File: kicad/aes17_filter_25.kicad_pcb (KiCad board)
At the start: 2 copper layers, 193 x 92.6 mm, 38 parts, among them J1 NC3FAAH, J2 NC3MAAH, J3 Conn_01x01_Pin, J4 Conn_01x01_Pin, SW1 SW_DPST, SW2 SW_DPDT_x2

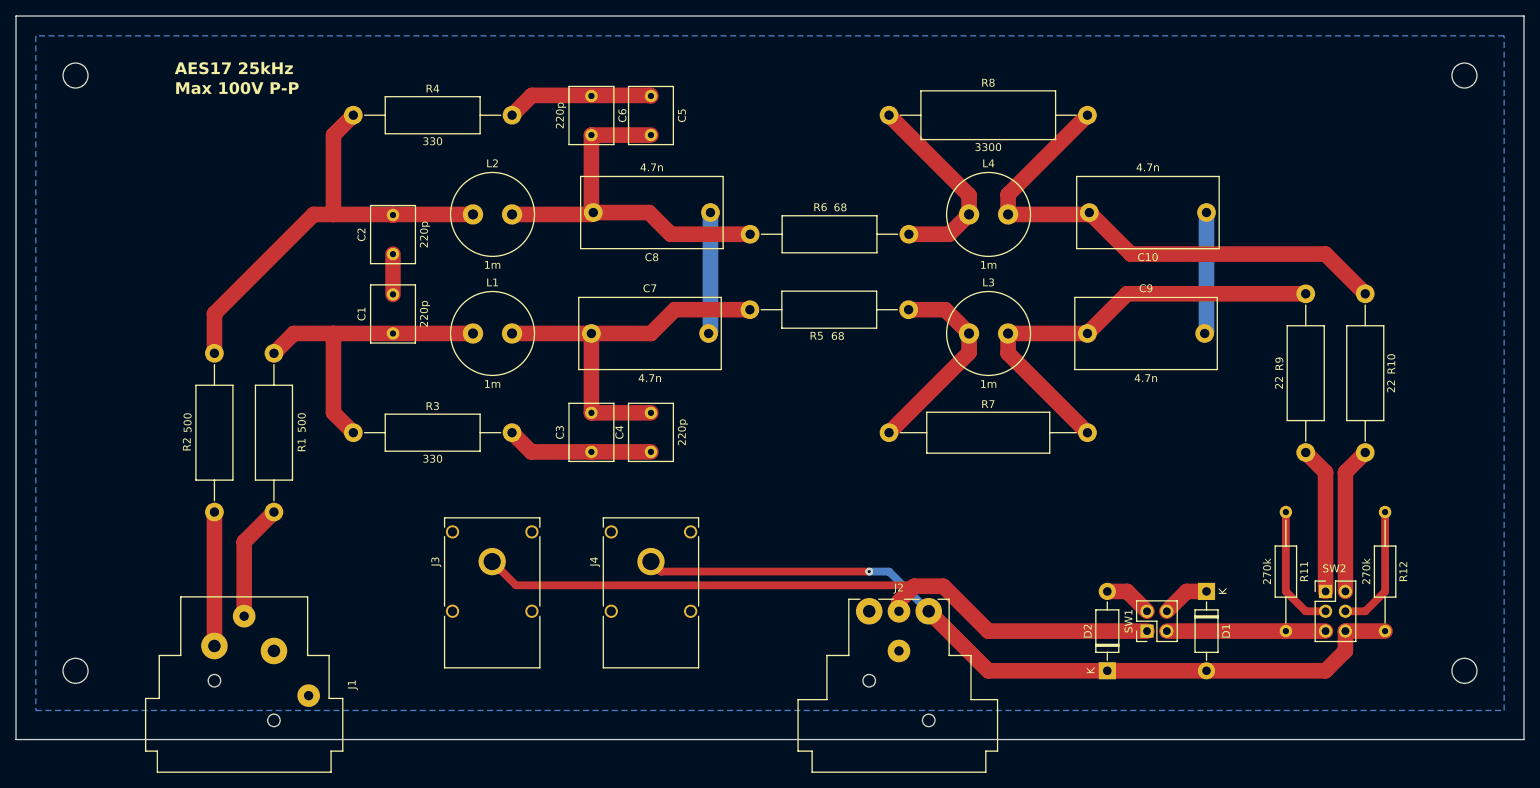
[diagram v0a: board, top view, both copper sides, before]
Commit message: Added GND connections to capacitor mid-points
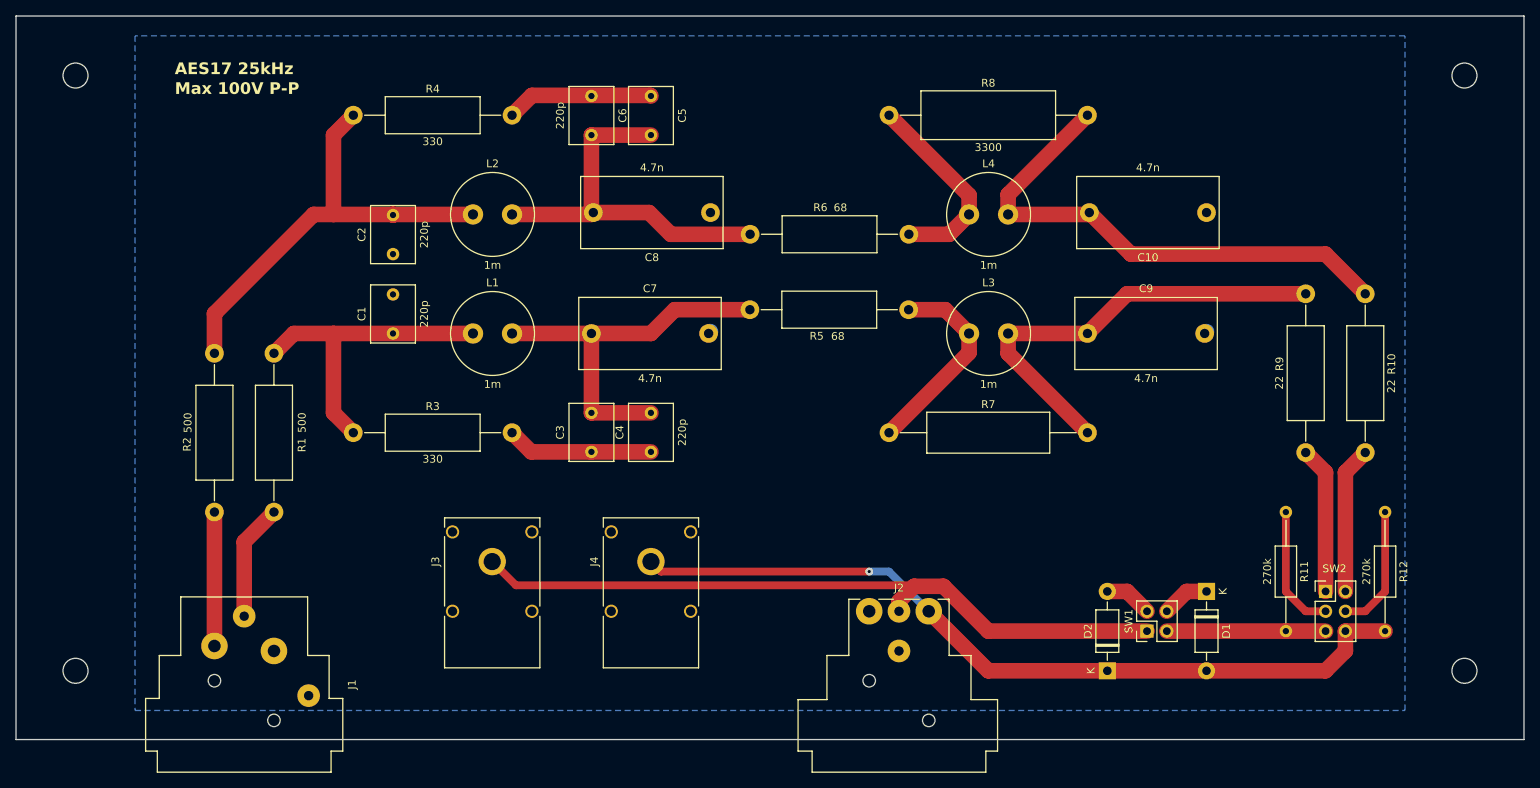
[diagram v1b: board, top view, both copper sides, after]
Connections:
- C1 pad 2: Net-(C1-Pad2) -> GND
- C10 pad 1: Net-(C10-Pad1) -> GND
- C2 pad 1: Net-(C1-Pad2) -> GND
- C7 pad 2: Net-(C7-Pad2) -> GND
- C8 pad 1: Net-(C7-Pad2) -> GND
- C9 pad 2: Net-(C10-Pad1) -> GND
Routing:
- net Net-(C7-Pad2): track 15.6 -> 0.00 mm
- net Net-(C10-Pad1): track 15.6 -> 0.00 mm
- net Net-(C1-Pad2): track 5.16 -> 0.00 mm
- net GND: track 0.00 -> 0.68 mm

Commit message: Readme updated
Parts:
- J1: value NC3FAAH -> NC3FAAH2
- R7: footprint Resistor_THT:R_Axial_DIN0516_L15.5mm_D5.0mm_P25.40mm_Horizontal -> Resistor_THT:R_Axial_DIN0414_L11.9mm_D4.5mm_P20.32mm_Horizontal
- R8: footprint Resistor_THT:R_Axial_DIN0617_L17.0mm_D6.0mm_P25.40mm_Horizontal -> Resistor_THT:R_Axial_DIN0414_L11.9mm_D4.5mm_P20.32mm_Horizontal
- moved H1 3.59 mm to (58.4, 55.9)
- moved H2 2.54 mm to (233.7, 55.9)
- moved H3 2.54 mm to (58.4, 129.5)
- moved R7 2.54 mm to (162.6, 99.1)
- moved R8 2.54 mm to (162.6, 58.4)
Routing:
- net Net-(SW2B-B): track 18.8 -> 22.9 mm
- net Net-(SW2A-B): track 18.8 -> 22.9 mm
- net Net-(SW2B-C): track 16.3 -> 12.3 mm
- net Net-(SW2A-C): track 16.3 -> 12.3 mm
- net Net-(C10-Pad2): track 67.0 -> 69.0 mm
- net Net-(L3-Pad1): track 25.9 -> 27.9 mm
- net Net-(L4-Pad1): track 25.7 -> 27.6 mm
- net Net-(C9-Pad1): track 57.1 -> 59.0 mm
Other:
- board size 193 x 92.6 mm -> 190 x 90 mm
- board text added: "AES17 25KHz 0.1dB variation 20Hz-40KHz -55dB at 250KHz Max 100V P-P into any load Max 200V P-P into R500+ (c) Matt Clark 2023 CERN-OHL-W PCB 190x90mm"
- board text removed: "AES17 25kHz"
- board text removed: "Max 100V P-P"

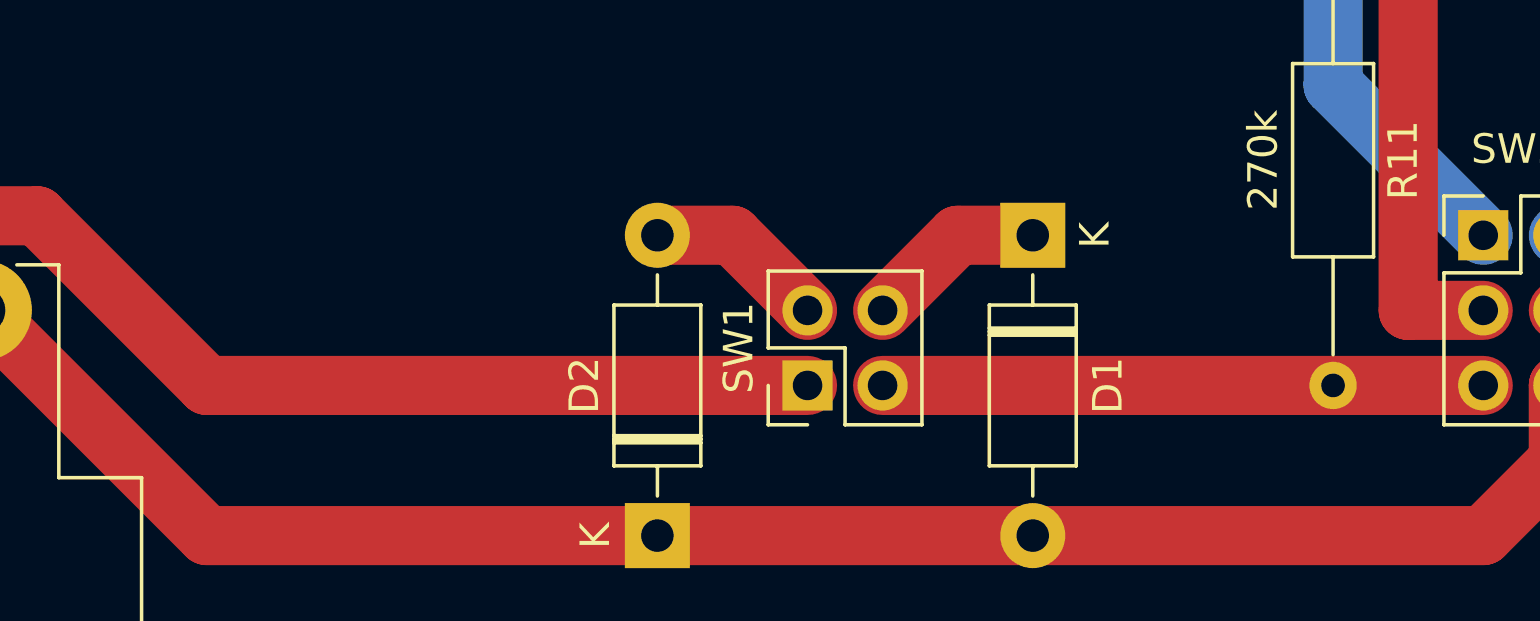
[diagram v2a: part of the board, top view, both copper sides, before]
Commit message: simplified diode switch to 1pst, fixed R7 and R8 footprints
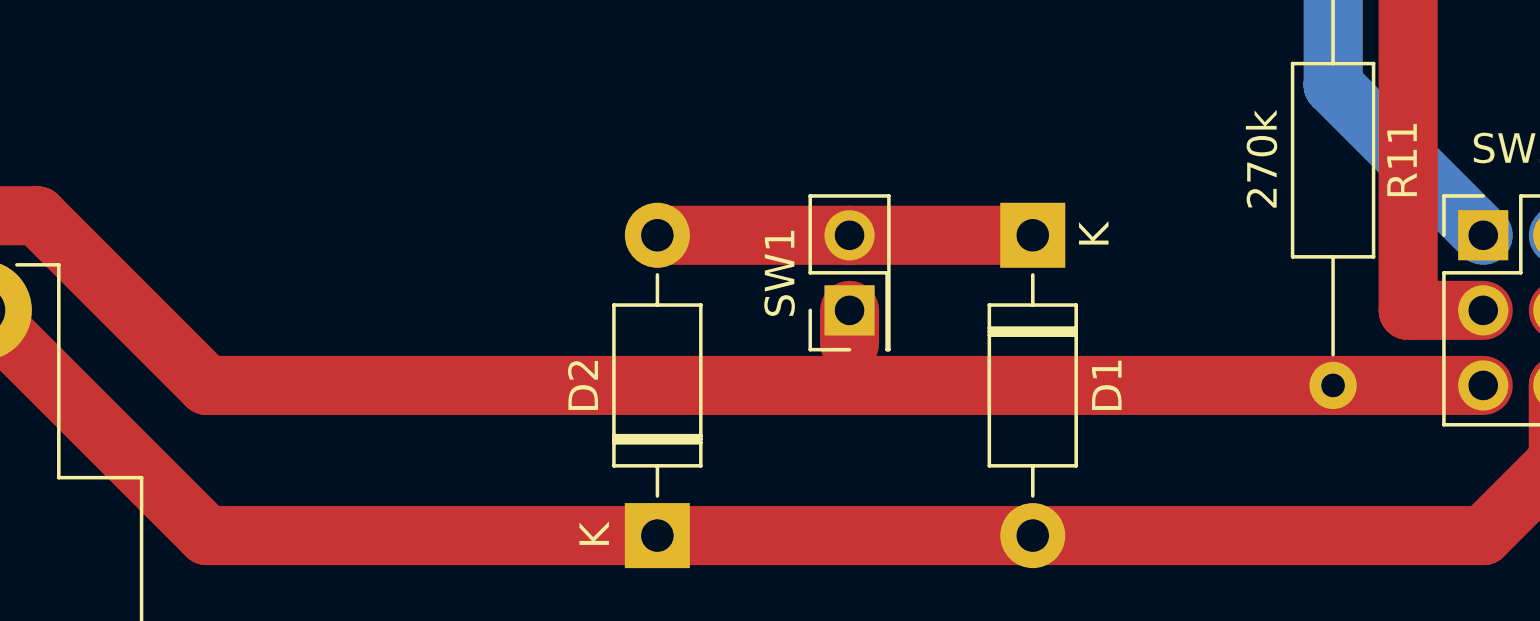
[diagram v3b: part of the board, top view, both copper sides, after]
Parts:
- J1: value NC3FAAH2 -> NC3FAAH
- SW1: value SW_DPST -> SW_SPST; footprint Connector_PinHeader_2.54mm:PinHeader_2x02_P2.54mm_Vertical -> Connector_PinHeader_2.54mm:PinHeader_2x01_P2.54mm_Vertical
- moved SW1 2.91 mm to (194.5, 121.9)
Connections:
- D2 pad 2: Net-(D2-A) -> Net-(D1-K)
- J1 pad G: unconnected-(J1-PadG) -> GND
- J2 pad G: unconnected-(J2-PadG) -> GND
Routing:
- net Net-(D1-K): track 6.13 -> 12.7 mm
- net Net-(D2-A): track 6.13 -> 0.00 mm
- net Net-(J3-Pin_1): track 112.9 -> 116.6 mm

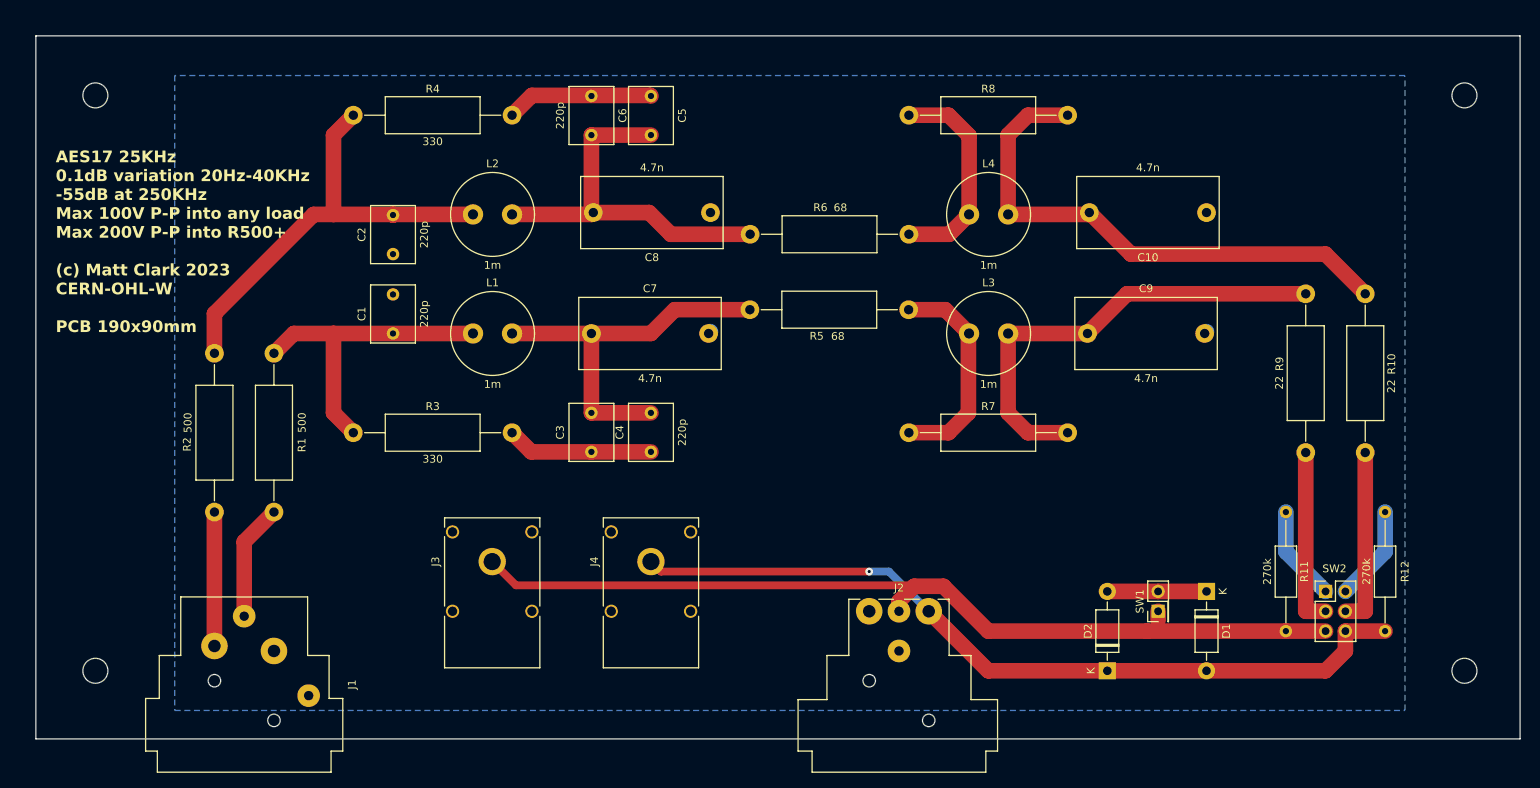
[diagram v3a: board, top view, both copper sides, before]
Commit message: Removed protection diodes, updated readme
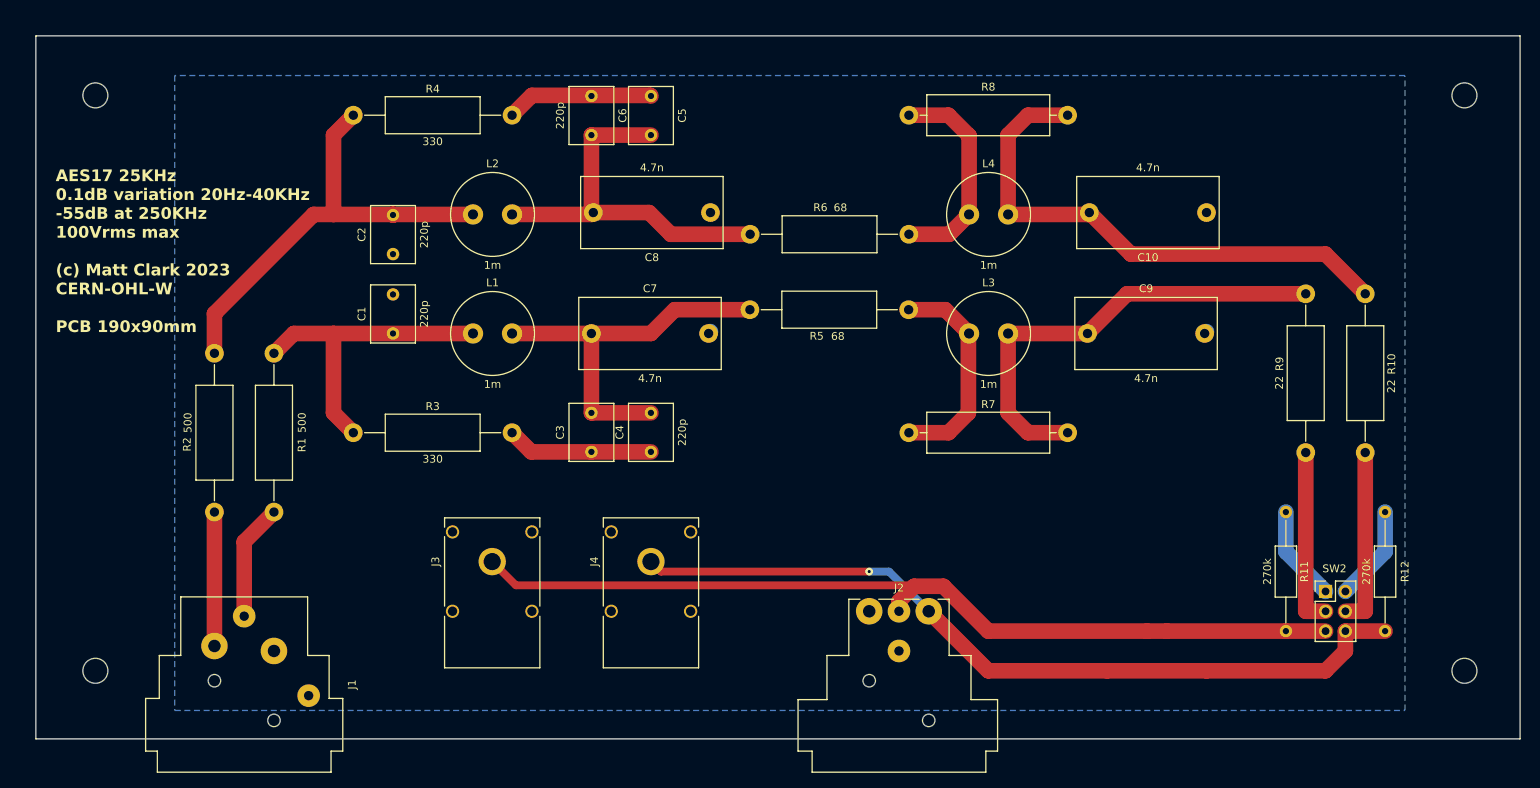
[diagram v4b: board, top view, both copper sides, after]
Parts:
- removed D1, D2: D_Zener, Diode_THT:D_DO-41_SOD81_P10.16mm_Horizontal
- removed SW1: SW_SPST, Connector_PinHeader_2.54mm:PinHeader_2x01_P2.54mm_Vertical
- R7, R8: footprint Resistor_THT:R_Axial_DIN0414_L11.9mm_D4.5mm_P20.32mm_Horizontal -> Resistor_THT:R_Axial_DIN0516_L15.5mm_D5.0mm_P20.32mm_Horizontal
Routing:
- net Net-(D1-K): track 12.7 -> 0.00 mm
- net Net-(J3-Pin_1): track 116.6 -> 115.4 mm
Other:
- board text added: "AES17 25KHz 0.1dB variation 20Hz-40KHz -55dB at 250KHz 100Vrms max (c) Matt Clark 2023 CERN-OHL-W PCB 190x90mm"
- board text removed: "AES17 25KHz 0.1dB variation 20Hz-40KHz -55dB at 250KHz Max 100V P-P into any load Max 200V P-P into R500+ (c) Matt Clark 2023 CERN-OHL-W PCB 190x90mm"

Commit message: Shrank board width, added images, updated readme
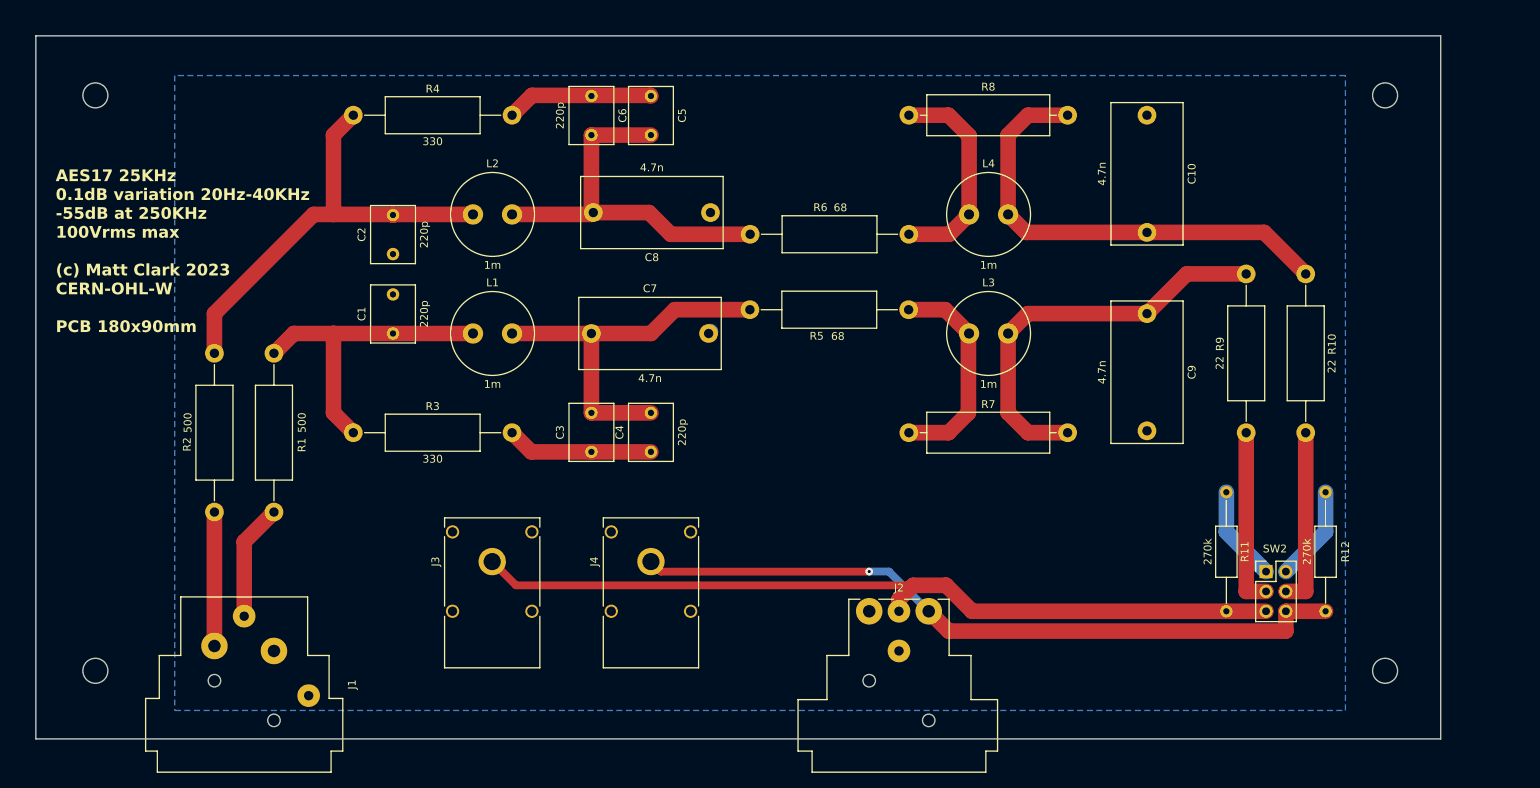
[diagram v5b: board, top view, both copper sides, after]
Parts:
- moved C10 14.6 mm to (193.0, 58.4), turned to -90 degrees
- moved H2 10.2 mm to (223.5, 55.9)
- moved H4 10.2 mm to (223.5, 129.5)
- moved C9 8.03 mm to (193.0, 83.8), turned to -90 degrees
- moved R9 8.03 mm to (205.7, 78.7)
- moved R11 8.03 mm to (203.2, 106.7)
- moved R12 8.03 mm to (215.9, 106.7)
- moved SW2 8.03 mm to (208.3, 116.8)
- moved R10 8.03 mm to (213.4, 78.7)
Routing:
- net Net-(J4-Pin_1): track 103.4 -> 92.6 mm
- net Net-(J3-Pin_1): track 115.4 -> 105.8 mm
- net Net-(C10-Pad2): track 69.0 -> 60.1 mm
- net Net-(C9-Pad1): track 59.0 -> 52.5 mm
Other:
- board size 190 x 90 mm -> 179.8 x 90 mm
- board text added: "AES17 25KHz 0.1dB variation 20Hz-40KHz -55dB at 250KHz 100Vrms max (c) Matt Clark 2023 CERN-OHL-W PCB 180x90mm"
- board text removed: "AES17 25KHz 0.1dB variation 20Hz-40KHz -55dB at 250KHz 100Vrms max (c) Matt Clark 2023 CERN-OHL-W PCB 190x90mm"
